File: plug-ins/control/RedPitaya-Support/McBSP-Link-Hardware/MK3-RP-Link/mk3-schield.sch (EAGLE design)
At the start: 16 parts, among them U1 SN65MLVD202A, U2 SN65MLVD202A, U3 SN65MLVD202A

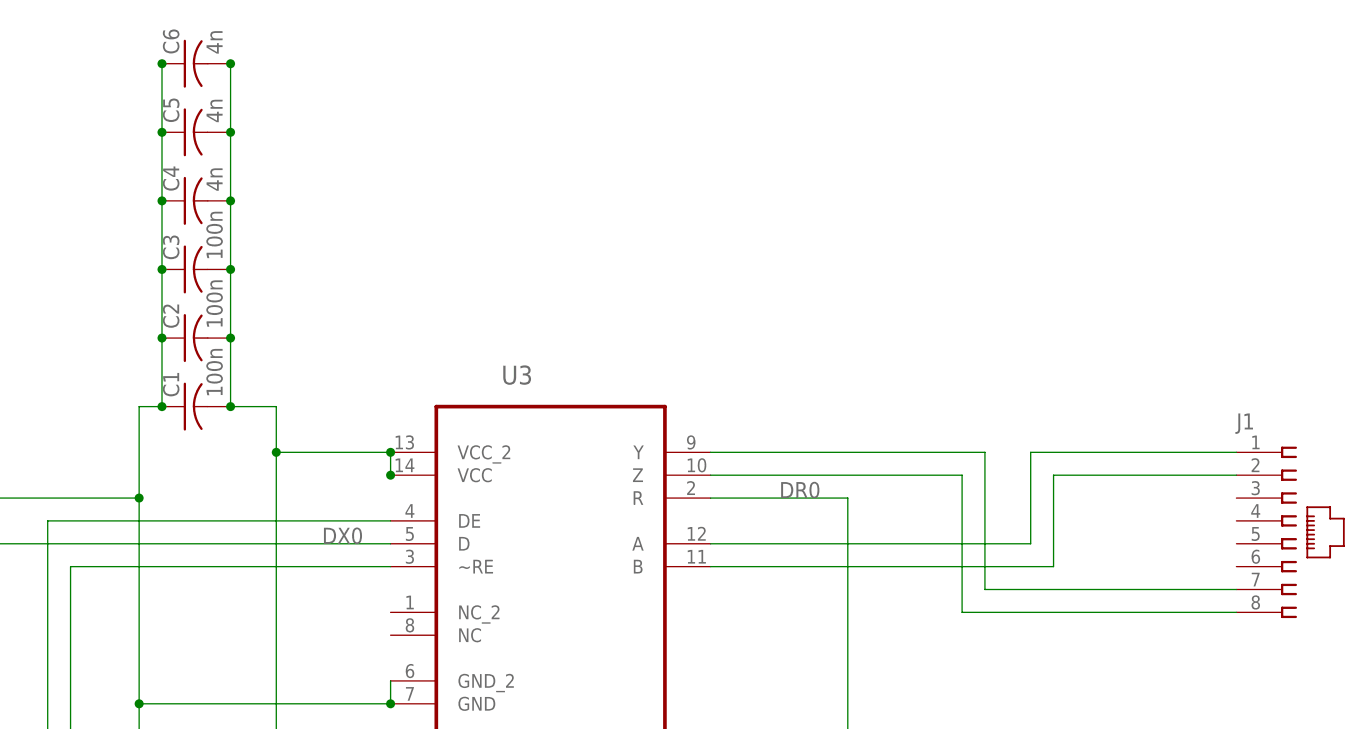
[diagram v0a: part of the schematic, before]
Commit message: updated gnd routing
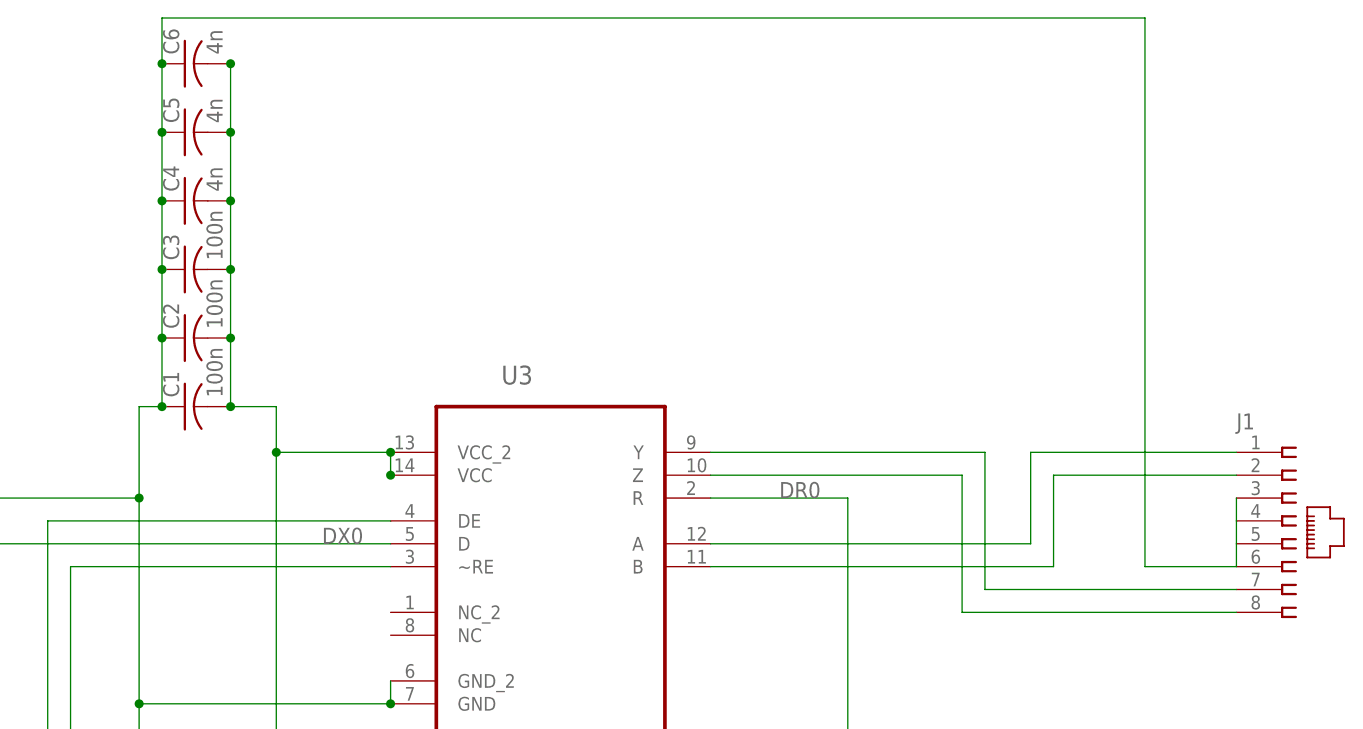
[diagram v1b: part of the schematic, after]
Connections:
- net GND: now also J1.3, J1.4, J1.5, J1.6
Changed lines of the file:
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@@
 <junction x="-33.02" y="-5.08"/>
 <label x="-45.72" y="2.54" size="1.778" layer="95"/>
+<pinref part="J1" gate="G$1" pin="3"/>
+<pinref part="J1" gate="G$1" pin="4"/>
+<wire x1="111.76" y1="121.92" x2="111.76" y2="119.38" width="0.1524" layer="91"/>
+<pinref part="J1" gate="G$1" pin="5"/>
+<wire x1="111.76" y1="119.38" x2="111.76" y2="116.84" width="0.1524" layer="91"/>
+<pinref part="J1" gate="G$1" pin="6"/>
+<wire x1="111.76" y1="116.84" x2="111.76" y2="114.3" width="0.1524" layer="91"/>
+<wire x1="111.76" y1="114.3" x2="101.6" y2="114.3" width="0.1524" layer="91"/>
+<wire x1="101.6" y1="114.3" x2="101.6" y2="175.26" width="0.1524" layer="91"/>
+<wire x1="101.6" y1="175.26" x2="-7.62" y2="175.26" width="0.1524" layer="91"/>
+<wire x1="-7.62" y1="175.26" x2="-7.62" y2="170.18" width="0.1524" layer="91"/>
 </segment>
 </net>
